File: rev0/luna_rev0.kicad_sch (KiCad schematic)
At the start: 19 parts, among them J1 USB_C_Receptacle_USB2.0, J2 USB_C_Receptacle_USB2.0, J3 USB_A, J4 USB_C_Receptacle_USB2.0, J7 PMOD_A, J8 PMOD_B, SW1 BTN_DFU, SW2 BTN_RESET, SW3 BTN_BTN

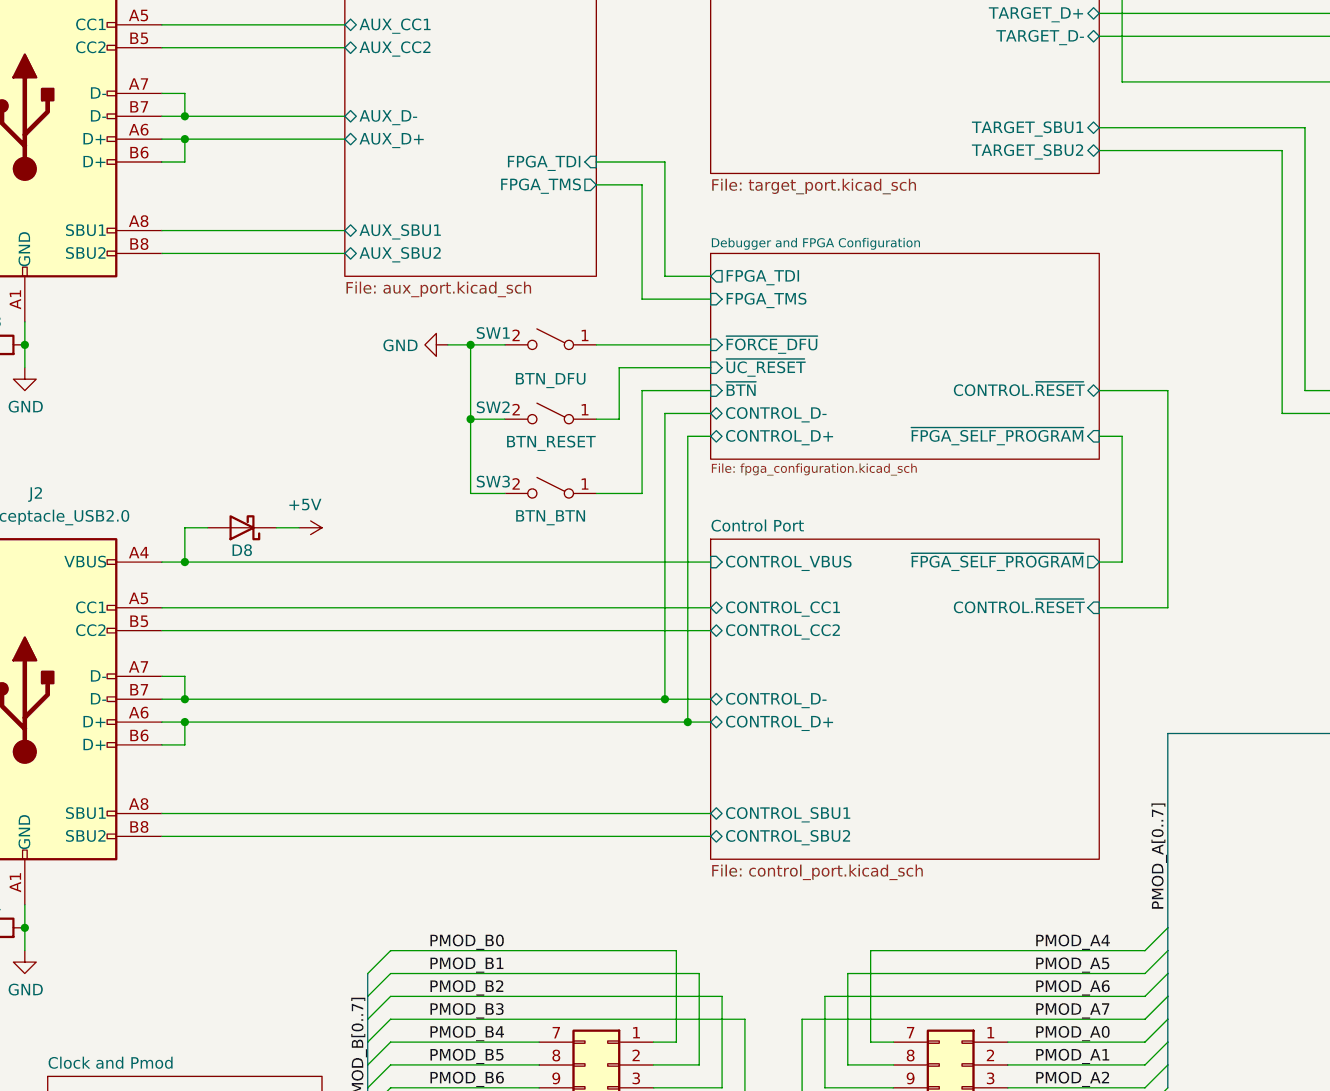
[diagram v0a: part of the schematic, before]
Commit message: hardware: add Control port USB switch
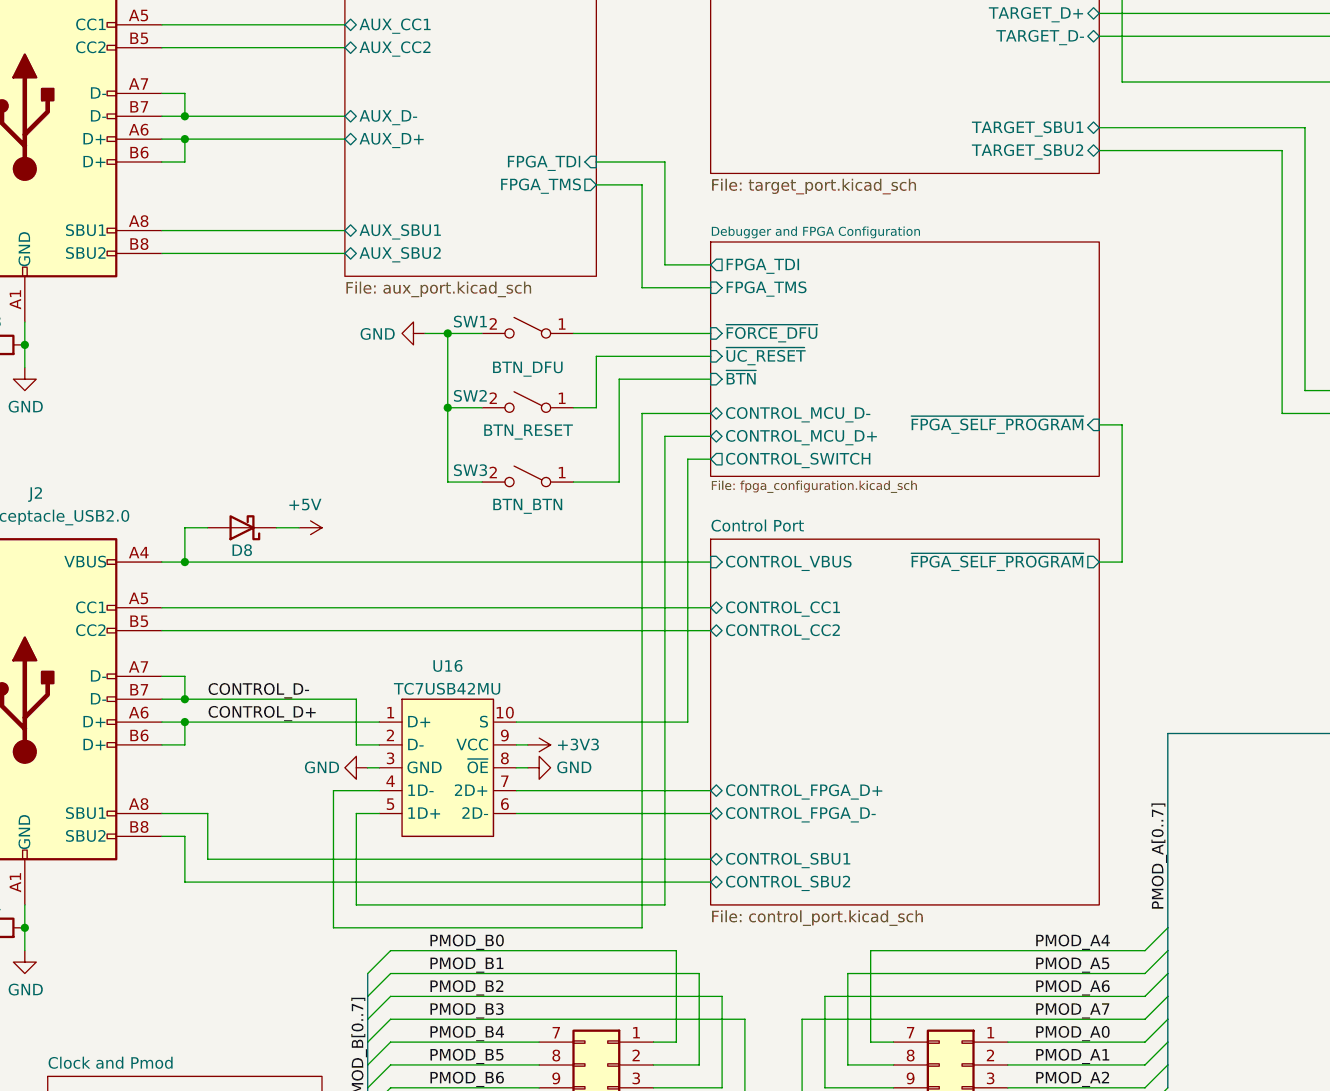
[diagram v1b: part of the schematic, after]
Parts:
- added U16: TC7USB42MU, symbol usb:TC7USB42MU
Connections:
- net +3V3: now also U16.9 (VCC)
- net GND: now also U16.3 (GND), U16.8 (~{OE})
- net Control Port/CONTROL_D+ renamed CONTROL_D+
- net CONTROL_D+: now also U16.1 (D+)
- net Control Port/CONTROL_D- renamed CONTROL_D-
- net CONTROL_D-: now also U16.2 (D-)
- new net Control Port/CONTROL_FPGA_D+: U16.7 (2D+)
- new net Control Port/CONTROL_FPGA_D-: U16.6 (2D-)
- new net Debugger and FPGA Configuration/CONTROL_MCU_D+: U16.5 (1D+)
- new net Debugger and FPGA Configuration/CONTROL_MCU_D-: U16.4 (1D-)
- new net Debugger and FPGA Configuration/CONTROL_SWITCH: U16.10 (S)
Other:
- sheet Control Port ports: added CONTROL_FPGA_D+, CONTROL_FPGA_D-; removed CONTROL.~{RESET}, CONTROL_D+, CONTROL_D-
- sheet Debugger and FPGA Configuration ports: added CONTROL_MCU_D+, CONTROL_MCU_D-, CONTROL_SWITCH; removed CONTROL.~{RESET}, CONTROL_D+, CONTROL_D-
- moved on the sheet: SW1, SW2, SW3

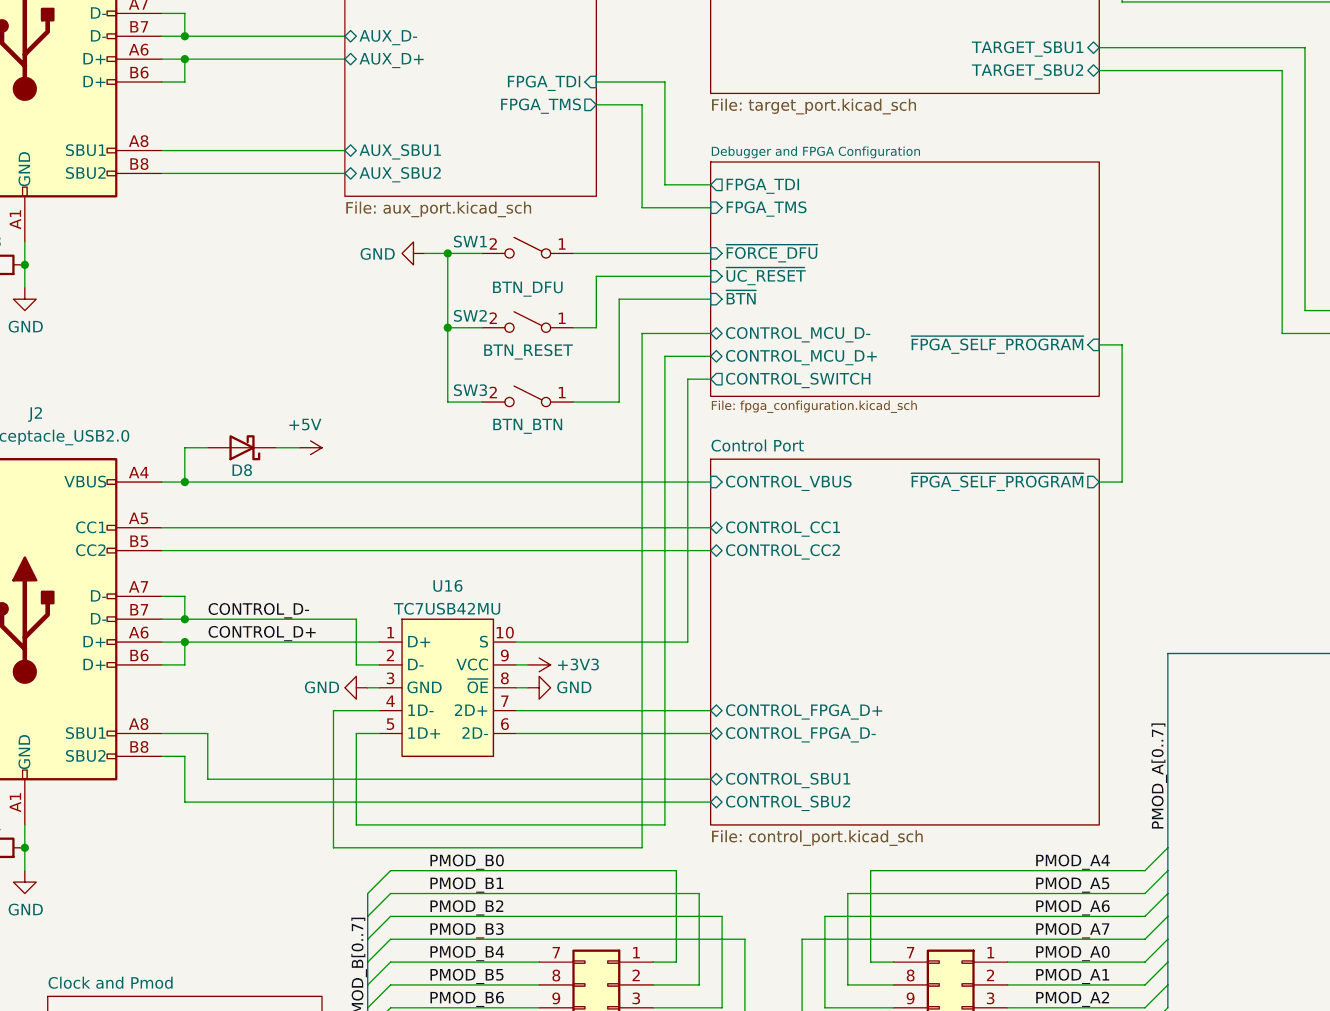
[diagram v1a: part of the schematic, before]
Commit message: hardware: add Control port reset detection
USB reset can be detected by measuring the D+/D- common-mode voltage
with the microcontroller's ADC or analog comparator.
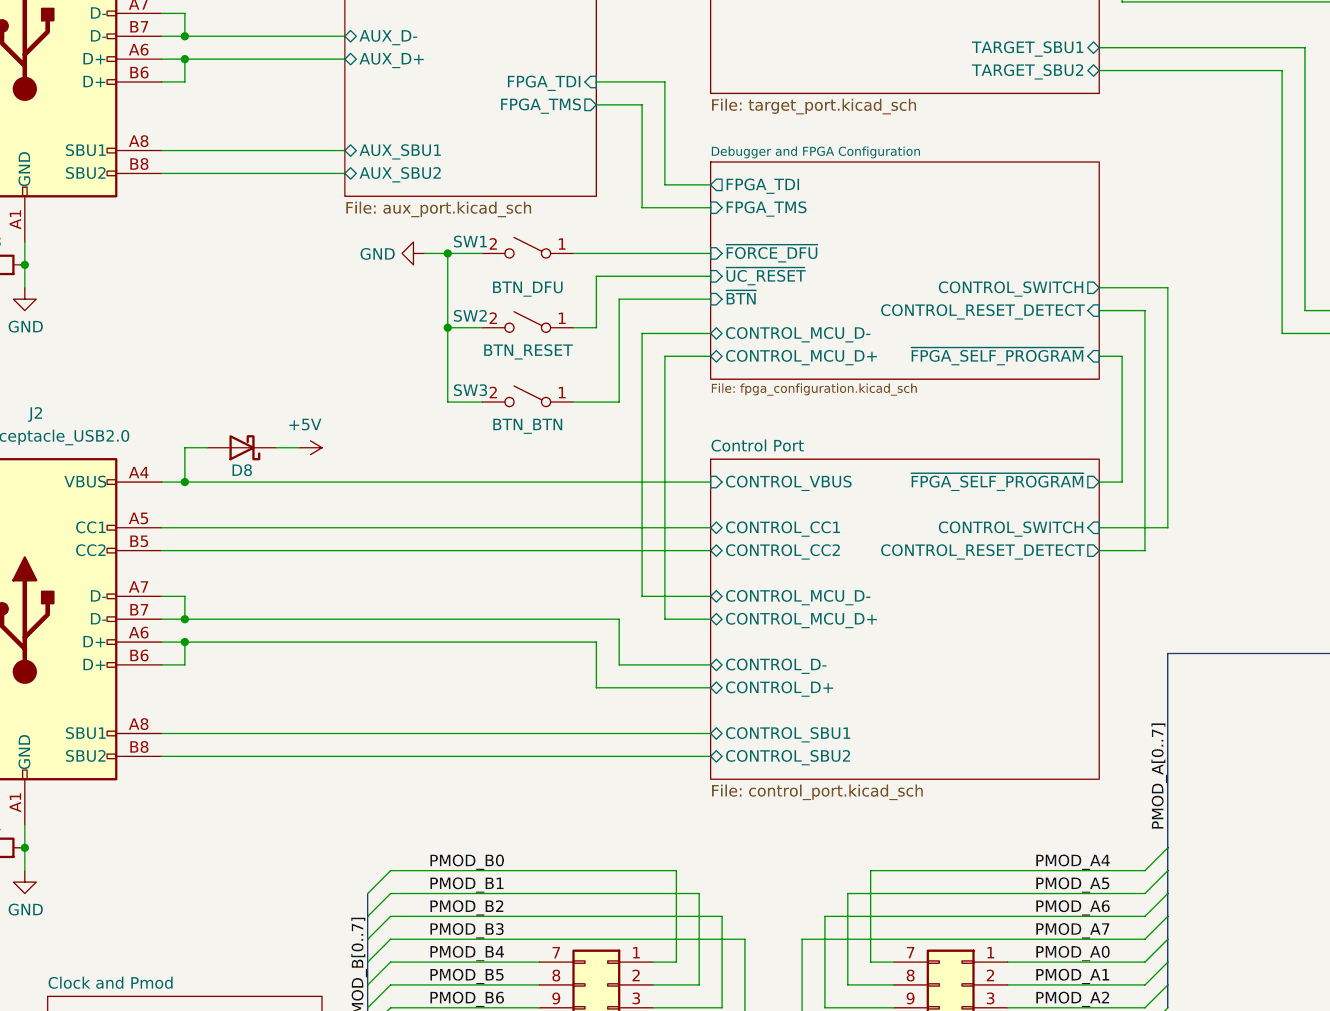
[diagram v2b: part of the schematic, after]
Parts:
- removed U16: TC7USB42MU, symbol usb:TC7USB42MU
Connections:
- net CONTROL_D+ renamed Control Port/CONTROL_D+
- net CONTROL_D- renamed Control Port/CONTROL_D-
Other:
- sheet Control Port ports: added CONTROL_D+, CONTROL_D-, CONTROL_MCU_D+, CONTROL_MCU_D-, CONTROL_RESET_DETECT, CONTROL_SWITCH; removed CONTROL_FPGA_D+, CONTROL_FPGA_D-
- sheet Debugger and FPGA Configuration ports: added CONTROL_RESET_DETECT; removed none

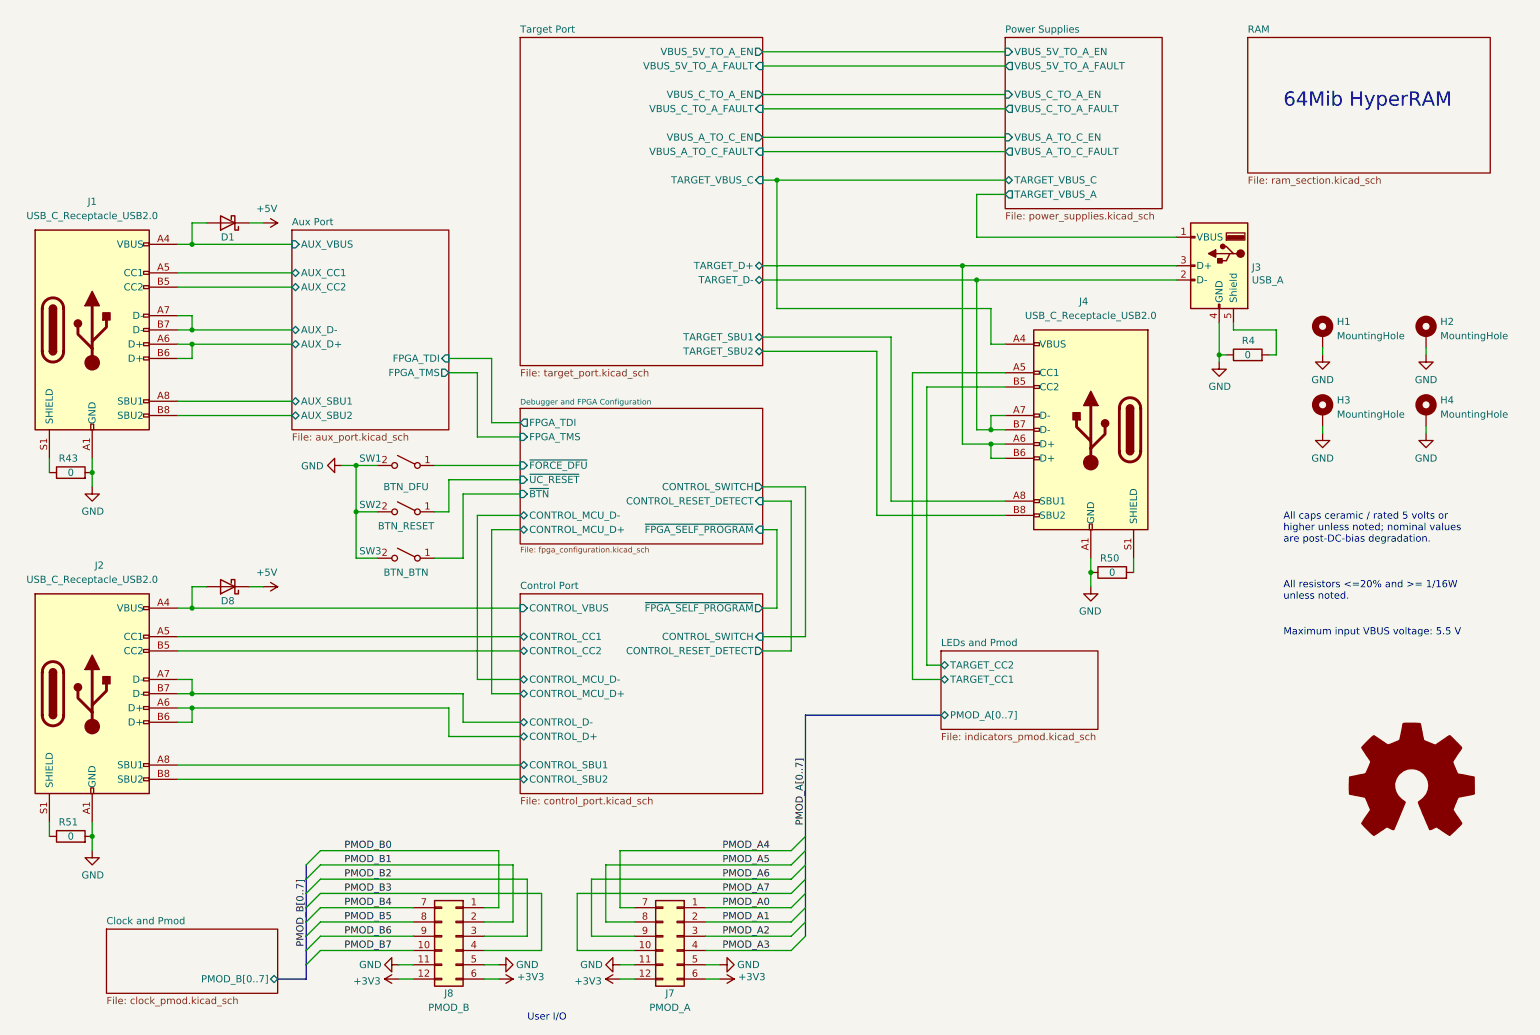
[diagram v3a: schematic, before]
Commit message: hardware: replace VBUS pass-through switches
- increase maximum voltage with discrete FET solution
- pass through Control and Aux VBUS directly, not +5V supply rail
- add current sense resistors
- eliminate discharge current of previous power switches
- eliminate possible overvoltage condition of previous power switches
- remove 10 uF VBUS output capacitor C53
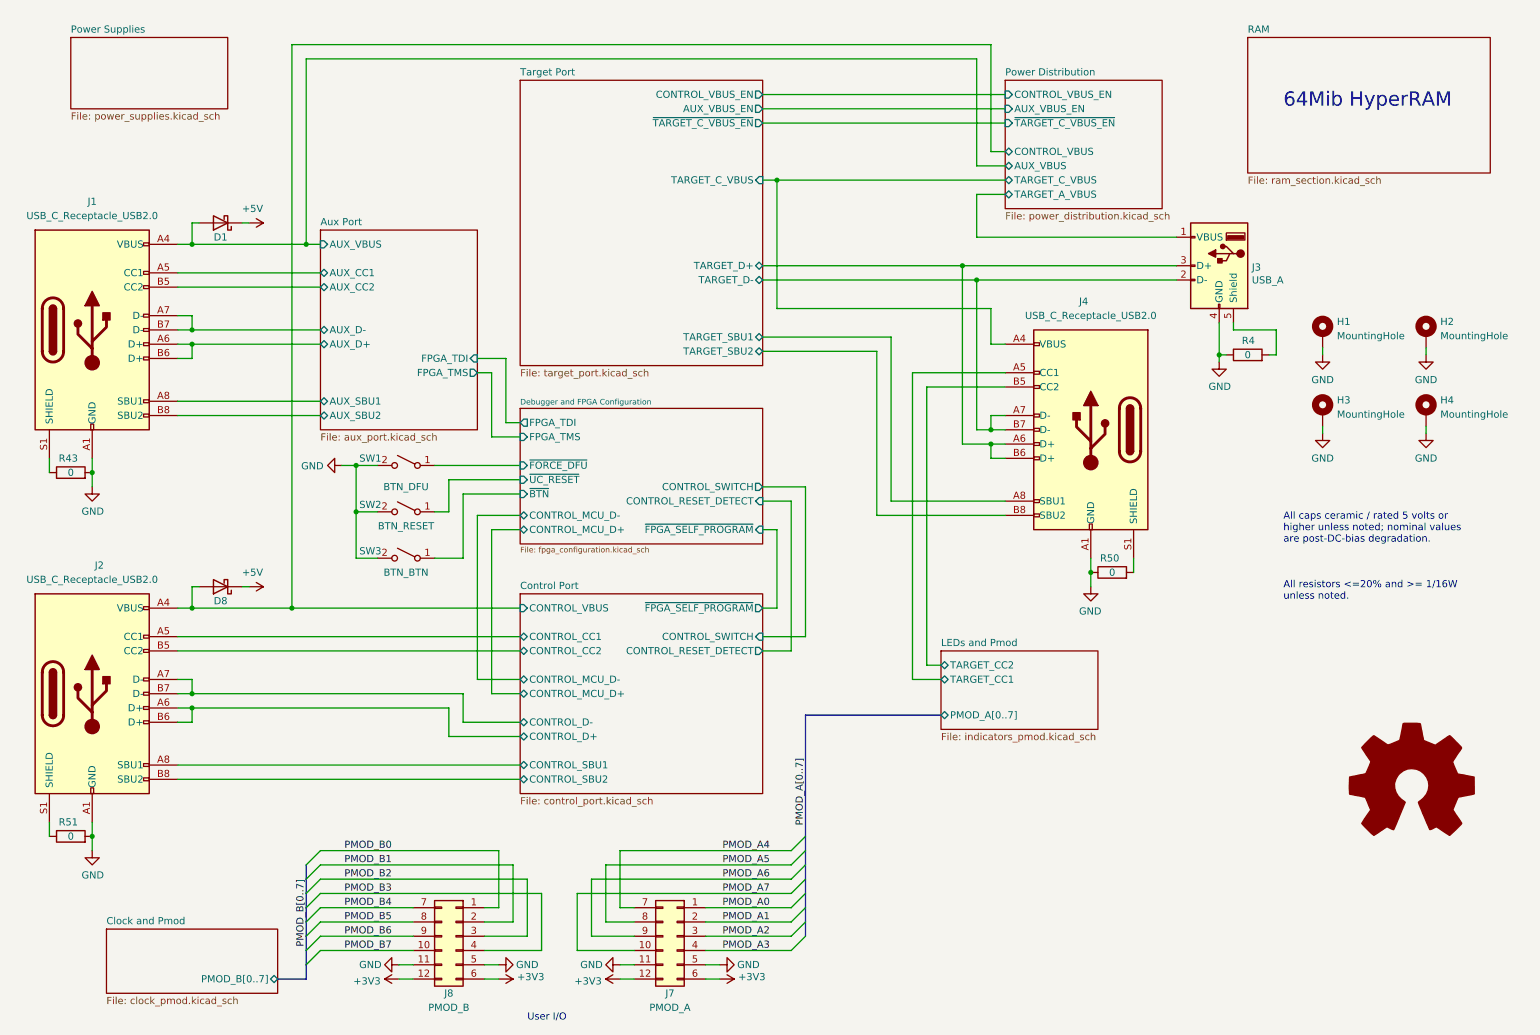
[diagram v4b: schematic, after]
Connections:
- net Power Supplies/TARGET_VBUS_A renamed Power Distribution/TARGET_A_VBUS
- net Power Supplies/TARGET_VBUS_C renamed Power Distribution/TARGET_C_VBUS
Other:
- added sheet Power Distribution (power_distribution.kicad_sch)
- sheet Power Supplies ports: added none; removed TARGET_VBUS_A, TARGET_VBUS_C, VBUS_5V_TO_A_EN, VBUS_5V_TO_A_FAULT, VBUS_A_TO_C_EN, VBUS_A_TO_C_FAULT, VBUS_C_TO_A_EN, VBUS_C_TO_A_FAULT
- sheet Target Port ports: added AUX_VBUS_EN, CONTROL_VBUS_EN, TARGET_C_VBUS, ~{TARGET_C_VBUS_EN}; removed TARGET_VBUS_C, VBUS_5V_TO_A_EN, VBUS_5V_TO_A_FAULT, VBUS_A_TO_C_EN, VBUS_A_TO_C_FAULT, VBUS_C_TO_A_EN, VBUS_C_TO_A_FAULT
- note removed: "Maximum input VBUS voltage: 5.5 V"
- moved on the sheet: D1, D8
